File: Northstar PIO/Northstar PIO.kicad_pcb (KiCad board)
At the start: 2 copper layers, 76.3 x 139.9 mm, 43 parts, among them J1 Conn_01x02, J1A1 CONFIG.HDR., J2 Conn_01x02, J3 Conn_01x02, J4 Conn_01x02, J5 Conn_01x02, J6 Conn_01x02, J7 Conn_02x15_Odd_Even, P1 INPUT PORT, P2 OUTPUT PORT, U1B1 LS74, U1C1 LS74, U1D1 LS164, U2A1 LS32, U2B1 LS138, U2C1 LS175, U2D1 LS03, U2E1 LS367, U3A1 LS14, U3B1 7437, U3C1 LS373, U3D1 LS373

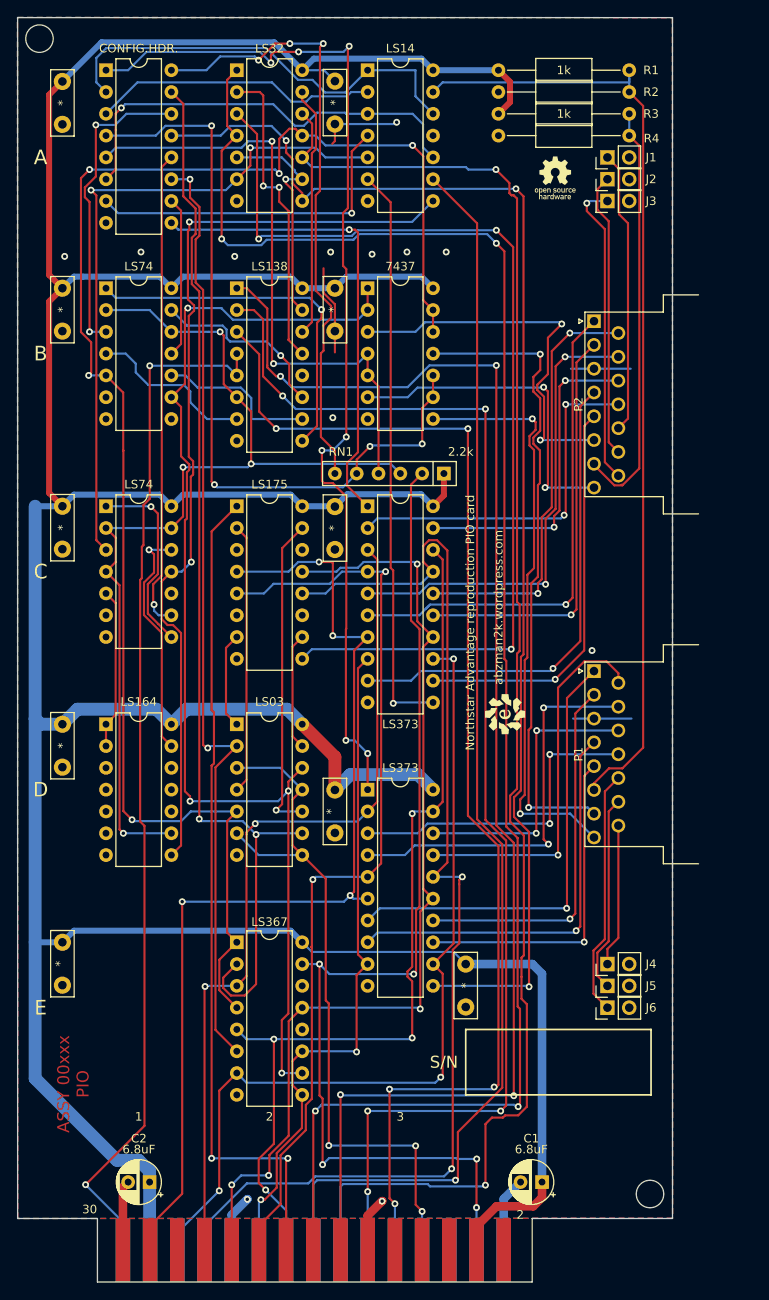
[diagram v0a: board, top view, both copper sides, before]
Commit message: revised PIO to use mouser DA15 parts
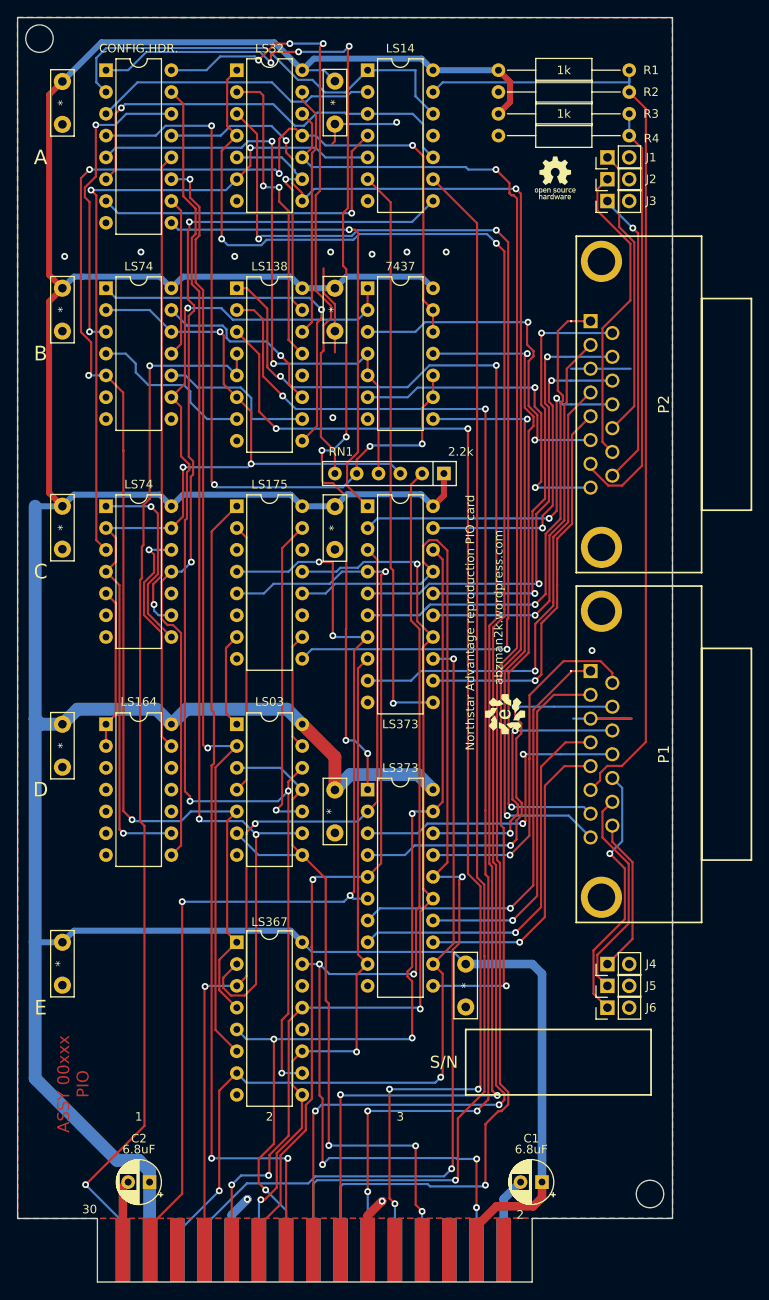
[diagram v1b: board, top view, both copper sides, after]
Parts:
- P1, P2: footprint Connector_Dsub:DSUB-15_Female_Horizontal_P2.77x2.84mm_EdgePinOffset9.40mm -> Evan's misc parts:L77SDA15S1ACH3R
- moved P1 0.40 mm to (145.1, 103.9)
- moved P2 0.40 mm to (145.1, 63.2)
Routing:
- net GND: track 63.9 -> 68.7 mm
- net //OUT FLAG: track 44.8 -> 40.9 mm
- net /IO A1: track 152.4 -> 149.1 mm
- net /IO A2: track 145.4 -> 142.5 mm
- net //READ PI REGISTER: track 153.6 -> 150.8 mm
- net Net-(P1-Pad5): track 38.6 -> 35.8 mm
- net Net-(P1-Pad1): track 52.6 -> 50.0 mm
- net Net-(P2-Pad2): track 48.7 -> 46.1 mm
- net Net-(P1-Pad9): track 44.1 -> 41.6 mm
- net Net-(P1-Pad4): track 47.7 -> 45.2 mm
- net Net-(J2-Pad1): track 33.3 -> 35.7 mm
- net Net-(P2-Pad9): track 49.8 -> 52.1 mm
- net //BRD: track 178.5 -> 176.2 mm
- net Net-(J5-Pad1): track 22.9 -> 25.2 mm
- net /IO A0: track 164.4 -> 162.2 mm
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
